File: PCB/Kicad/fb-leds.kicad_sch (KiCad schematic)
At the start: 32 parts

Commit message: PDF
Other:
- note added: "FEEDBACK LEDS"
- moved on the sheet: D1, D10, D11, D12, D13, D14, D15, D2, D3, D4, D5, D6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

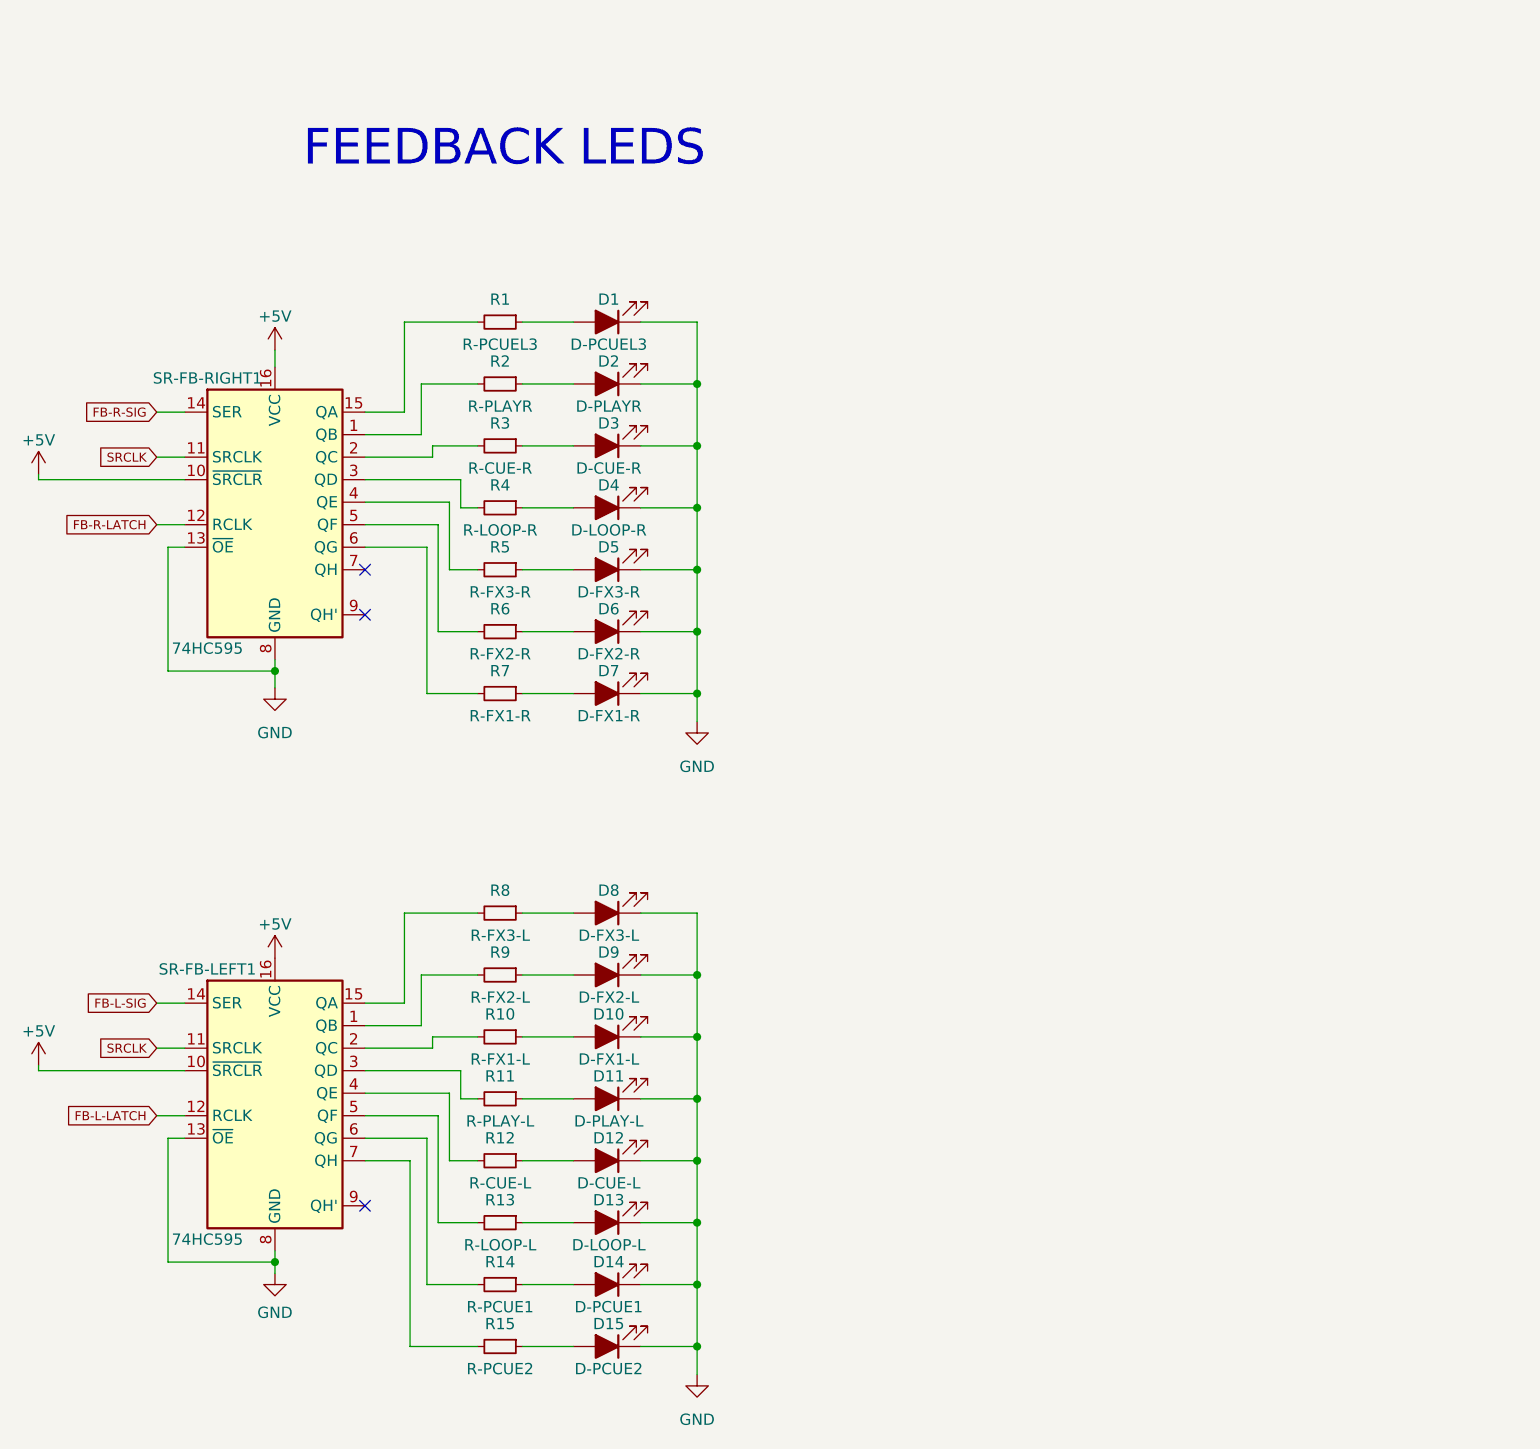
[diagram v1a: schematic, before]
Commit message: added transistor and 3x leds play- cue
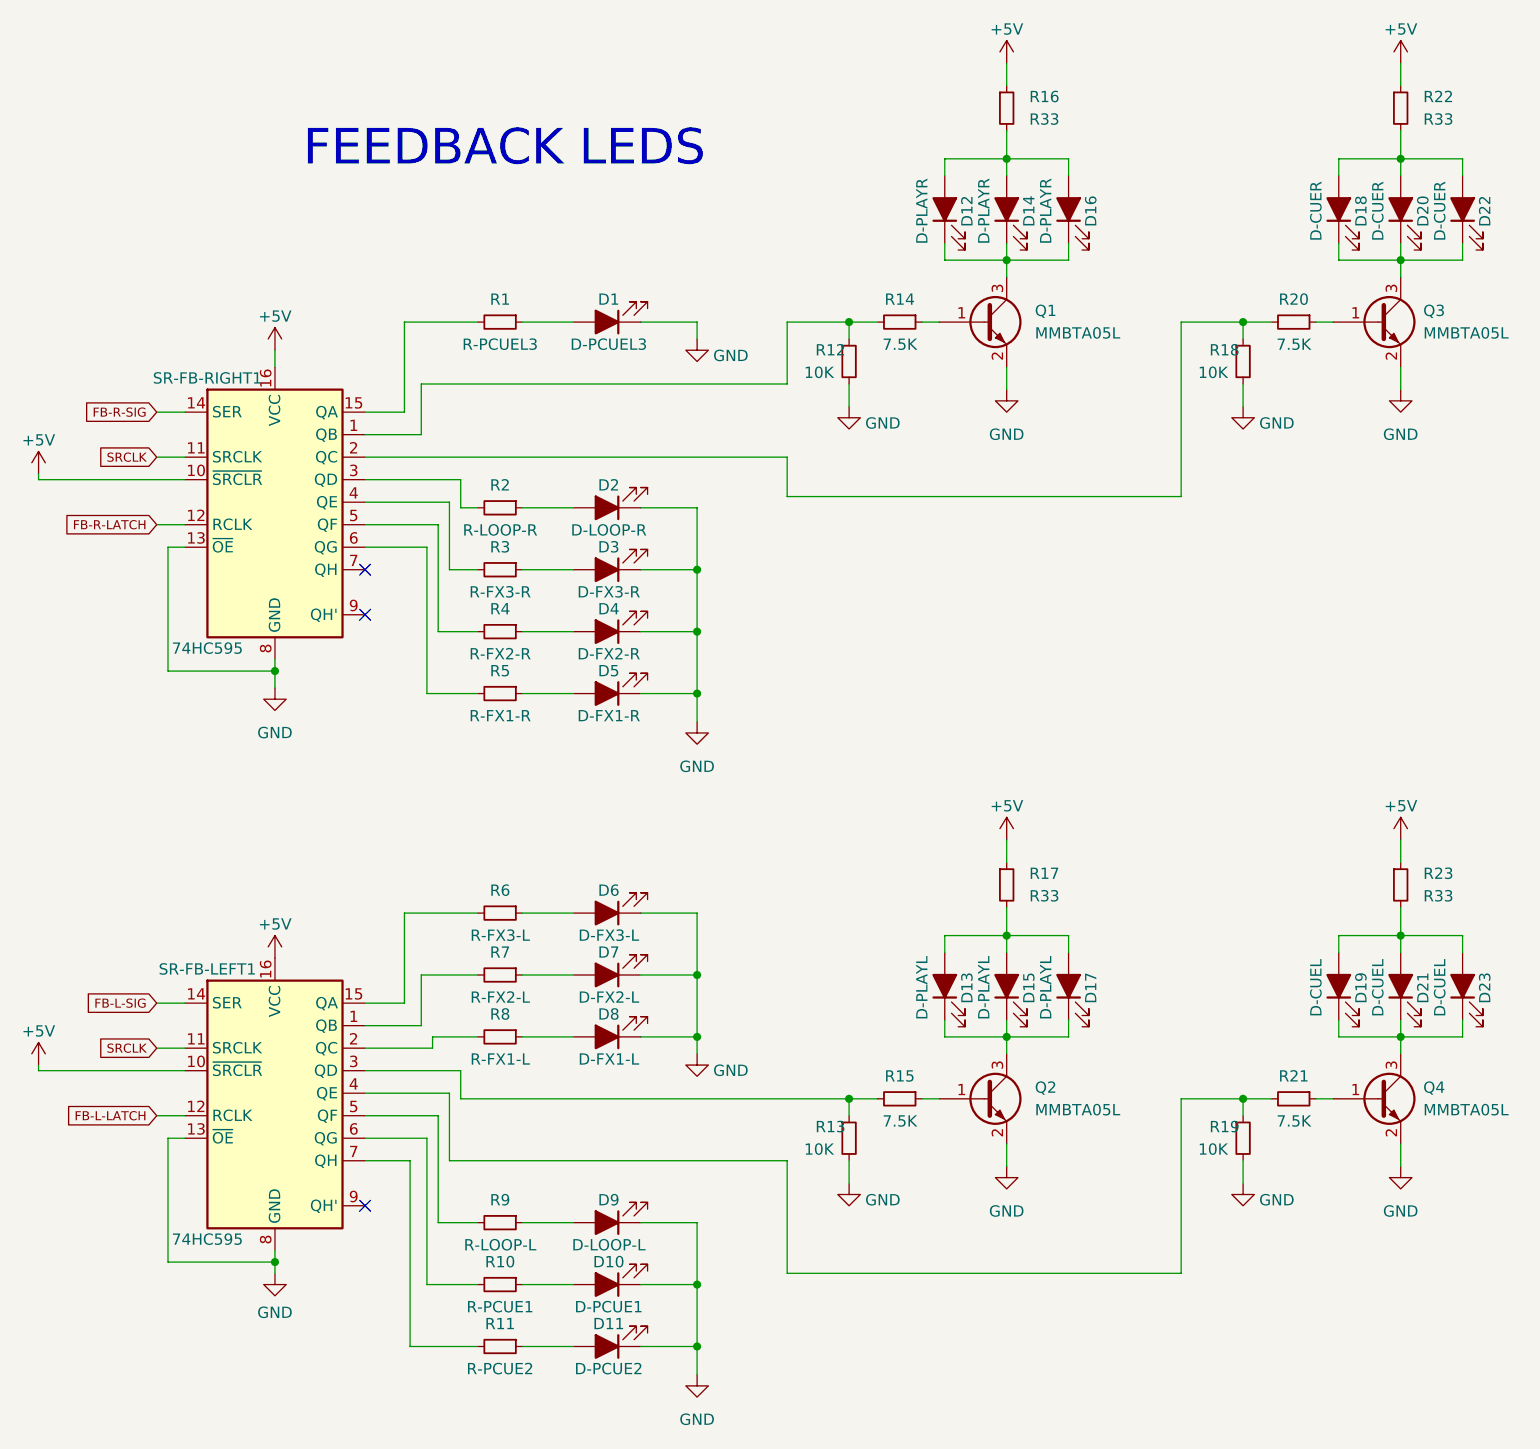
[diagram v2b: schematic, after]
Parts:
- removed D11: D-PLAY-L, Library:LED_GREEN, symbol Device:LED_Filled
- removed D12: D-CUE-L, Library:LED_GREEN, symbol Device:LED_Filled
- removed D3: D-CUE-R, Library:LED_GREEN, symbol Device:LED_Filled
- removed R11: R-PLAY-L, Library:R_1206_3216Metric_Pad1.30x1.75mm_HandSolder, symbol Device:R_Small
- removed R3: R-CUE-R, Library:R_1206_3216Metric_Pad1.30x1.75mm_HandSolder, symbol Device:R_Small
- added D13, D15, D17: D-PLAYL, Library:LED_1206_3216Metric_Pad1.42x1.75mm_HandSolder, symbol Device:LED_Filled
- added D14, D16: D-PLAYR, Library:LED_1206_3216Metric_Pad1.42x1.75mm_HandSolder, symbol Device:LED_Filled
- added D18, D20, D22: D-CUER, Library:LED_1206_3216Metric_Pad1.42x1.75mm_HandSolder, symbol Device:LED_Filled
- added D19, D21, D23: D-CUEL, Library:LED_1206_3216Metric_Pad1.42x1.75mm_HandSolder, symbol Device:LED_Filled
- added Q1, Q2, Q3, Q4: MMBTA05L, Library:SOT-23_Handsoldering, symbol Transistor_BJT:MMBTA42
- added R13, R18, R19: 10K, Library:R_1206_3216Metric_Pad1.30x1.75mm_HandSolder, symbol Device:R_Small
- added R15, R20, R21: 7.5K, Library:R_1206_3216Metric_Pad1.30x1.75mm_HandSolder, symbol Device:R_Small
- added R16, R17, R22, R23: R33, Library:R_1206_3216Metric_Pad1.30x1.75mm_HandSolder, symbol Device:R_Small
- D1: footprint Library:LED_GREEN -> Library:LED_1206_3216Metric_Pad1.42x1.75mm_HandSolder
- D10: renamed from D14; footprint Library:LED_GREEN -> Library:LED_1206_3216Metric_Pad1.42x1.75mm_HandSolder
- D11: renamed from D15; footprint Library:LED_GREEN -> Library:LED_1206_3216Metric_Pad1.42x1.75mm_HandSolder
- D12: renamed from D2; footprint Library:LED_GREEN -> Library:LED_1206_3216Metric_Pad1.42x1.75mm_HandSolder
- D2: renamed from D4; footprint Library:LED_GREEN -> Library:LED_1206_3216Metric_Pad1.42x1.75mm_HandSolder
- D3: renamed from D5; footprint Library:LED_GREEN -> Library:LED_1206_3216Metric_Pad1.42x1.75mm_HandSolder
- D4: renamed from D6; footprint Library:LED_GREEN -> Library:LED_1206_3216Metric_Pad1.42x1.75mm_HandSolder
- D5: renamed from D7; footprint Library:LED_GREEN -> Library:LED_1206_3216Metric_Pad1.42x1.75mm_HandSolder
- D6: renamed from D8; footprint Library:LED_GREEN -> Library:LED_1206_3216Metric_Pad1.42x1.75mm_HandSolder
- D7: renamed from D9; footprint Library:LED_GREEN -> Library:LED_1206_3216Metric_Pad1.42x1.75mm_HandSolder
- D8: renamed from D10; footprint Library:LED_GREEN -> Library:LED_1206_3216Metric_Pad1.42x1.75mm_HandSolder
- D9: renamed from D13; footprint Library:LED_GREEN -> Library:LED_1206_3216Metric_Pad1.42x1.75mm_HandSolder
- R12: value R-CUE-L -> 10K
- R14: renamed from R2; value R-PLAYR -> 7.5K
- renumbered R14 to R10, R15 to R11, R4 to R2, R5 to R3, R6 to R4, R7 to R5, R8 to R6, R9 to R7, R10 to R8, R13 to R9
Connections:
- net +5V: now also R16.1, R17.1, R22.1, R23.1
- net GND: now also R12.2, Q1.2 (E), Q2.2 (E), Q3.2 (E), Q4.2 (E), R13.2, R18.2, R19.2; no longer D12.1 (K)
- net at SR-FB-LEFT1.3 (QD): now also R13.1, R15.2
- net at SR-FB-LEFT1.4 (QE): now also R19.1, R21.2; no longer R12.2
- net at R14.2, SR-FB-RIGHT1.1 (QB): now also R12.1
- net at SR-FB-RIGHT1.2 (QC): now also R18.1, R20.2
- net at D12.2 (A): now also D14.2 (A), D16.2 (A), R16.2; no longer R14.1
- new net: D18.1 (K), D20.1 (K), D22.1 (K), Q3.3 (C)
- new net: D18.2 (A), D20.2 (A), D22.2 (A), R22.2
- new net: Q4.1 (B), R21.1
- new net: Q1.1 (B), R14.1
- new net: D12.1 (K), D14.1 (K), D16.1 (K), Q1.3 (C)
- new net: D19.2 (A), D21.2 (A), D23.2 (A), R23.2
- new net: Q2.1 (B), R15.1
- new net: D19.1 (K), D21.1 (K), D23.1 (K), Q4.3 (C)
- new net: Q3.1 (B), R20.1
- new net: D13.1 (K), D15.1 (K), D17.1 (K), Q2.3 (C)
- new net: D13.2 (A), D15.2 (A), D17.2 (A), R17.2
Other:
- moved on the sheet: D12, R14

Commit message: routing WIP
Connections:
- net at SR-FB-LEFT1.6 (QG): now also R11.2; no longer R10.2
- net at SR-FB-LEFT1.7 (QH): now also R10.2; no longer R11.2
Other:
- moved on the sheet: D10, D11, R10, R11
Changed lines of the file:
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@@
     (pin "2")
   )
-  (symbol (lib_id "Device:R_Small") (at 124.46 161.925 270) (unit 1)
-    (in_bom yes) (on_board yes)
-    (property "Reference" "R10" (id 0) (at 124.46 159.385 90))
-    (property "Value" "R-PCUE1" (id 1) (at 124.46 164.465 90))
+  (symbol (lib_id "Device:R_Small") (at 124.46 161.925 270) (mirror x) (unit 1)
+    (in_bom yes) (on_board yes)
+    (property "Reference" "R11" (id 0) (at 124.46 164.465 90))
+    (property "Value" "R-PCUE2" (id 1) (at 124.46 159.385 90))
     (property "Footprint" "Library:R_1206_3216Metric_Pad1.30x1.75mm_HandSolder" (id 2) (at 124.46 161.925 0)
       (effects (font (size 1.27 1.27)) hide)
@@
     (pin "2")
   )
-  (symbol (lib_id "Device:R_Small") (at 124.46 168.91 270) (unit 1)
-    (in_bom yes) (on_board yes)
-    (property "Reference" "R11" (id 0) (at 124.46 166.37 90))
-    (property "Value" "R-PCUE2" (id 1) (at 124.46 171.45 90))
+  (symbol (lib_id "Device:R_Small") (at 124.46 168.91 270) (mirror x) (unit 1)
+    (in_bom yes) (on_board yes)
+    (property "Reference" "R10" (id 0) (at 124.46 171.45 90))
+    (property "Value" "R-PCUE1" (id 1) (at 124.46 166.37 90))
     (property "Footprint" "Library:R_1206_3216Metric_Pad1.30x1.75mm_HandSolder" (id 2) (at 124.46 168.91 0)
       (effects (font (size 1.27 1.27)) hide)
@@
     (pin "2")
   )
-  (symbol (lib_id "Device:LED_Filled") (at 136.525 161.925 180) (unit 1)
-    (in_bom yes) (on_board yes)
-    (property "Reference" "D10" (id 0) (at 136.7155 159.385 0))
-    (property "Value" "D-PCUE1" (id 1) (at 136.7155 164.465 0))
+  (symbol (lib_id "Device:LED_Filled") (at 136.525 161.925 0) (mirror y) (unit 1)
+    (in_bom yes) (on_board yes)
+    (property "Reference" "D11" (id 0) (at 136.7155 164.465 0))
+    (property "Value" "D-PCUE2" (id 1) (at 136.7155 159.385 0))
     (property "Footprint" "Library:LED_1206_3216Metric_Pad1.42x1.75mm_HandSolder" (id 2) (at 136.525 161.925 0)
       (effects (font (size 1.27 1.27)) hide)
@@
     (pin "2")
   )
-  (symbol (lib_id "Device:LED_Filled") (at 136.525 168.91 180) (unit 1)
-    (in_bom yes) (on_board yes)
-    (property "Reference" "D11" (id 0) (at 136.7155 166.37 0))
-    (property "Value" "D-PCUE2" (id 1) (at 136.7155 171.45 0))
+  (symbol (lib_id "Device:LED_Filled") (at 136.525 168.91 0) (mirror y) (unit 1)
+    (in_bom yes) (on_board yes)
+    (property "Reference" "D10" (id 0) (at 136.7155 171.45 0))
+    (property "Value" "D-PCUE1" (id 1) (at 136.7155 166.37 0))
     (property "Footprint" "Library:LED_1206_3216Metric_Pad1.42x1.75mm_HandSolder" (id 2) (at 136.525 168.91 0)
       (effects (font (size 1.27 1.27)) hide)

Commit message: routing WIP
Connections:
- net at R12.1, R14.2: now also SR-FB-RIGHT1.2 (QC); no longer SR-FB-RIGHT1.1 (QB)
- net at R18.1, R20.2: now also SR-FB-RIGHT1.1 (QB); no longer SR-FB-RIGHT1.2 (QC)
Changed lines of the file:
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@@
     (stroke (width 0) (type solid) (color 0 0 0 0))
   )
-  (wire (pts (xy 109.22 66.04) (xy 115.57 66.04))
-    (stroke (width 0) (type solid) (color 0 0 0 0))
-  )
-  (wire (pts (xy 109.22 68.58) (xy 156.845 68.58))
-    (stroke (width 0) (type solid) (color 0 0 0 0))
+  (wire (pts (xy 109.22 68.58) (xy 115.57 68.58))
+    (stroke (width 0) (type default) (color 0 0 0 0))
   )
   (wire (pts (xy 109.22 71.12) (xy 120.015 71.12))
@@
     (stroke (width 0) (type solid) (color 0 0 0 0))
   )
+  (wire (pts (xy 115.57 60.325) (xy 115.57 68.58))
+    (stroke (width 0) (type solid) (color 0 0 0 0))
+  )
   (wire (pts (xy 115.57 60.325) (xy 156.845 60.325))
     (stroke (width 0) (type solid) (color 0 0 0 0))
   )
-  (wire (pts (xy 115.57 66.04) (xy 115.57 60.325))
-    (stroke (width 0) (type solid) (color 0 0 0 0))
-  )
   (wire (pts (xy 115.57 127) (xy 121.92 127))
     (stroke (width 0) (type solid) (color 0 0 0 0))
@@
     (stroke (width 0) (type solid) (color 0 0 0 0))
   )
-  (wire (pts (xy 156.845 68.58) (xy 156.845 73.025))
-    (stroke (width 0) (type solid) (color 0 0 0 0))
-  )
+  (wire (pts (xy 156.845 66.04) (xy 109.22 66.04))
+    (stroke (width 0) (type default) (color 0 0 0 0))
+  )
+  (wire (pts (xy 156.845 66.04) (xy 156.845 73.025))
+    (stroke (width 0) (type solid) (color 0 0 0 0))
+  )

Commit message: routes finished
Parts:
- D1, D10, D11, D12, D13, D14, D15, D16, D17, D18, D19, D2, D20, D21, D22, D23, D3, D4, D5, D6, D7, D8, D9: footprint Library:LED_1206_3216Metric_Pad1.42x1.75mm_HandSolder -> LED_SMD:LED_1206_3216Metric_Pad1.42x1.75mm_HandSolder
